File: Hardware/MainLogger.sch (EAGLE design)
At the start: 193 parts, among them J3 GEMS_POWER_PLUGINPUT, J4 U.FL, J5 B_SERIES_M.2EKEY_3042, Q1 DMG3404, Q2 MOSFET_PCH-DMP3036SFG, Q3 MOSFET_PCH-DMP3036SFG, Q4 DMG3404, Q5 NX2301P, U1 FXMAR2102UMLP, U10 SIP32431TDFN, U11 LTC4412S6, U12 TCR2LE31ESV, U13 LP59073.3VYKE, U14 MIC22602, U15 BQ25616, U16 TPS61282D, U17 MCP23018QFN, U18 MCP23018QFN, U19 MAX-M8W, U2 VEML3328, U20 MCP79412SOIC, U21 HALL_EFFECT_SI7201, U22 PCA9634QFN, U23 SN74LVC1G17DCK, U24 TPL5010DDC, U25 TPL5010DDC, U26 MB85RC, U3 MMC5633, U4 MXC6655, U5 PAC1934QFN, U6 PAC1934QFN, U7 SN74AUP1G08DCK, U8 FXMAR2102UMLP, U9 SN74AUP3G34DCU

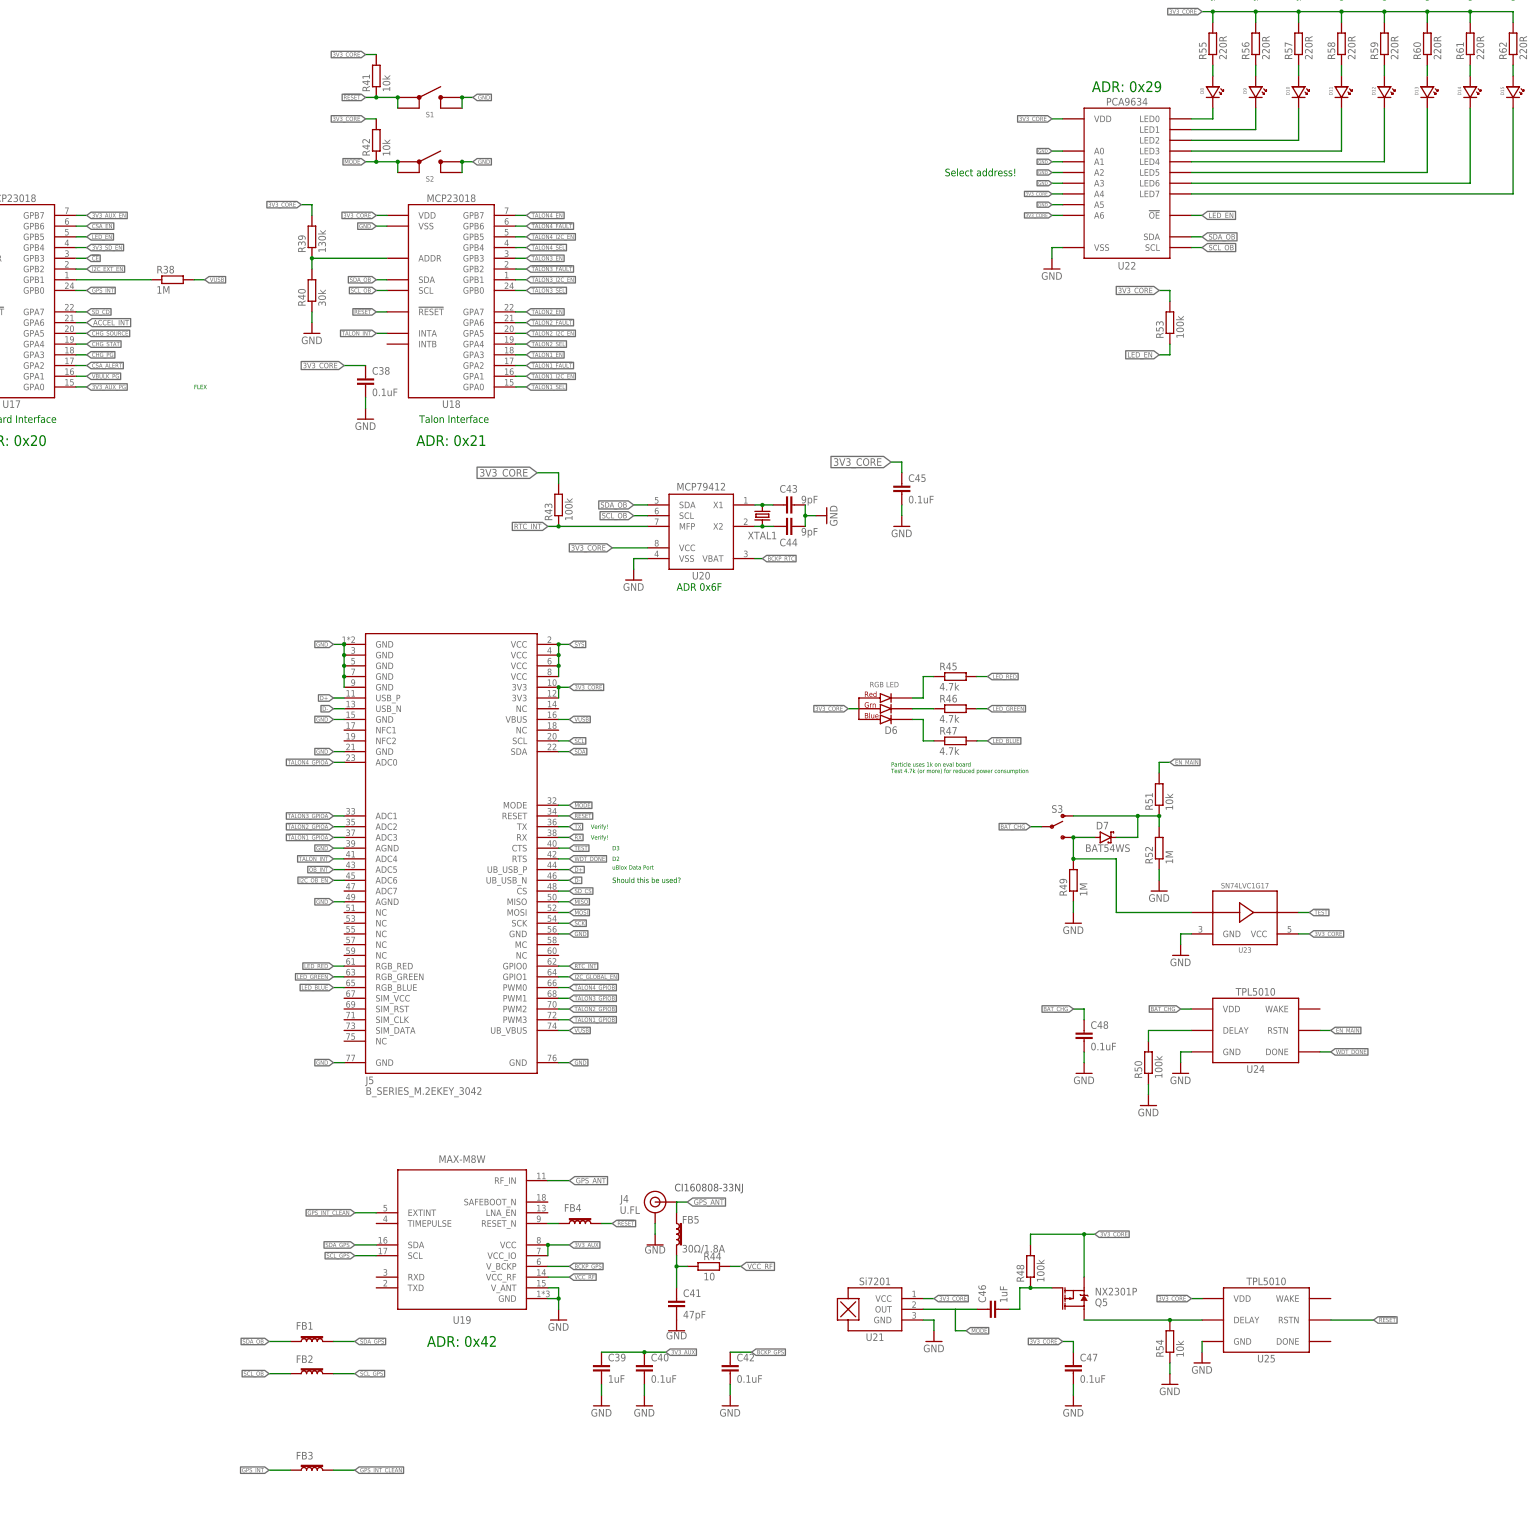
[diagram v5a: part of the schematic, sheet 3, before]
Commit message: v1.0 Update
Many fixes, see ECO and Github issues documentation, v1.0 sent to fab
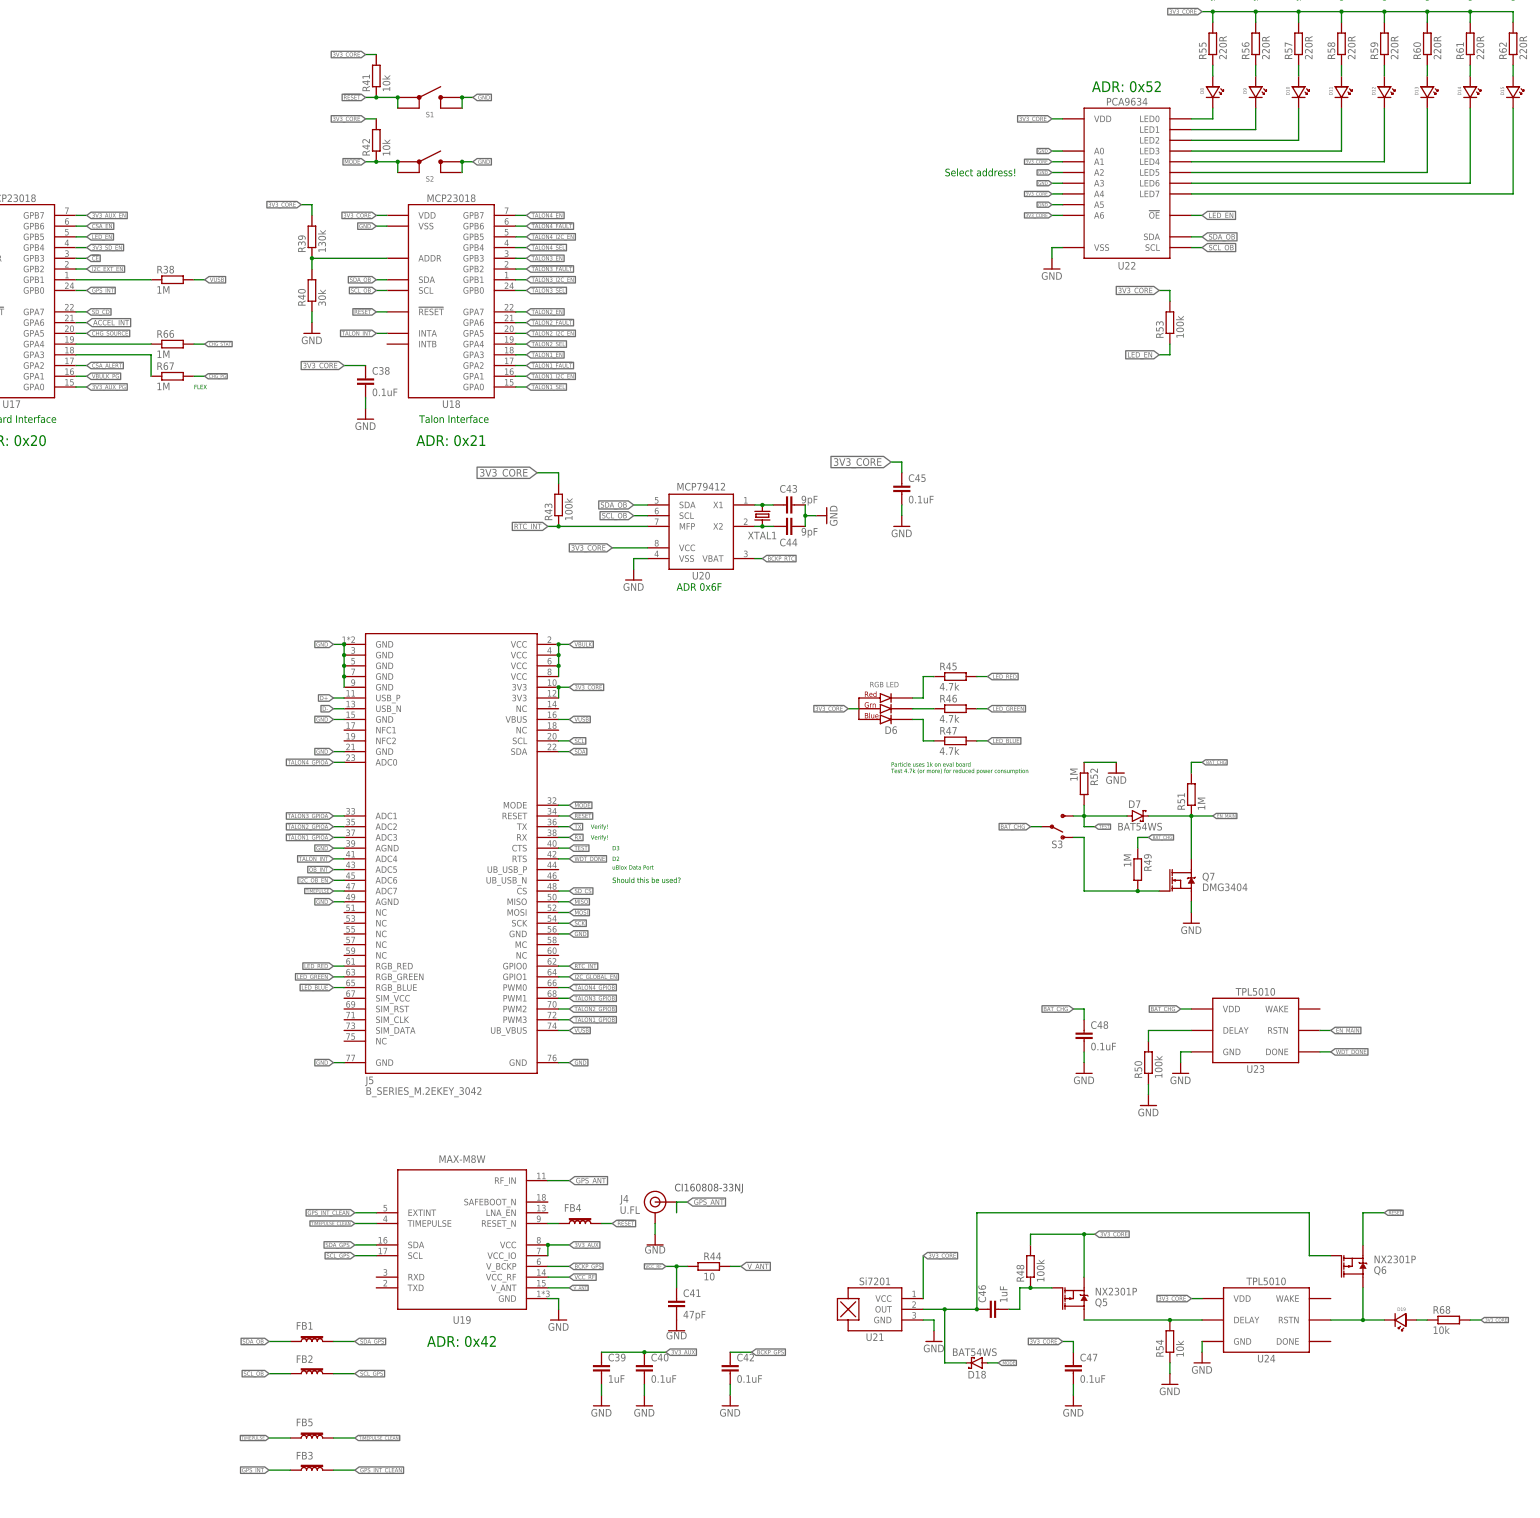
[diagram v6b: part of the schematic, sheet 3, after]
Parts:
- added C50: 0.1uF, bschulz_passives:C-EU0.1UFC0402
- added D17: (no value), bschulz:DIODE_CCBAT54CSOT23
- added D18: BAT54WS, bschulz:DIODE_SCHOTTKYSOD-323
- added D19: LEDGREEN0603, bschulz:LEDGREEN0603
- added Q6: NX2301P, bschulz:MOSFET-PCH-NX2301P
- added Q7: DMG3404, bschulz:MOSFET-NCH-DMG3404L
- added R65, R66, R67: 1M, bschulz_passives:R-EU_1MR0402
- added R68: 10k, bschulz_passives:R-EU_10KR0402
- FB5: value 30Ω/1.8A -> (none); device SparkFun-Coils:FERRITE_BEAD-0603 -> bschulz:FERRITE_BEAD1KS0402; DIGIKEY 445-2986-1-ND -> (none); MF TDK -> (none); MPN MPZ1608D300BTA00 -> (none)
- J3: value GEMS_POWER_PLUGINPUT -> GEMS_POWER_PLUGINPUT_RT; device bschulz:GEMS_POWER_PLUGINPUT -> bschulz:GEMS_POWER_PLUGINPUT_RT
- R51: value 10k -> 1M; device bschulz_passives:R-EU_10KR0402 -> bschulz_passives:R-EU_1MR0402
- S3: value SPDT7103K2CWA -> SPDT7103K2CWAV2; device bschulz:SPDT7103K2CWA -> bschulz:SPDT7103K2CWAV2
- U23: value SN74LVC1G17DCK -> TPL5010DDC; device bschulz:SN74LVC1G17DCK -> bschulz:TPL5010DDC
- U25: value TPL5010DDC -> MB85RC; device bschulz:TPL5010DDC -> bschulz:MB85RC
- U26: value MB85RC -> SHTC3DFN; device bschulz:MB85RC -> bschulz:SHTC3DFN
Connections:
- removed net ANT_VCC: C41.1, FB5.2, R44.1
- removed net N$29: D7.C, R51.1, R52.2, S3.O
- new net N$11: C46.1, D18.C, Q6.G, U21.OUT
- new net N$14: D19.ANODE, R68.1
- new net N$6: R66.1, U17.GPA4
- new net N$8: Q7.G, R49.2, S3.O
- new net N$9: R67.1, U17.GPA3
- new net STAT_CORE: D17.C, R30.2, R31.2, R33.2, R35.2
- new net TIMEPULSE: FB5.1, J5U1.ADC7
- new net TIMEPULSE_CLEAN: FB5.2, U19.TIMEPULSE
- new net V_ANT: R44.2, U19.V_ANT
- net !CHG_PG: now also R67.2; no longer U17.GPA3
- net !MODE: now also D18.A; no longer C46.1, U21.OUT
- net !RESET: now also Q6.S; no longer U25.RSTN
- net 3V3_AUX: now also C50.1, U26.VCC
- net 3V3_CORE: now also D17.A2, R68.2, U22.A1, U24.VDD; no longer U23.VCC, U26.A0, U26.A1, U26.A2, U26.VDD
- net BAT_CHG: now also R49.1, R51.2, U23.VDD; no longer U24.VDD
- net CHG_STAT: now also R66.2; no longer U17.GPA4
- net D+: no longer J5U1.UB_USB_P, U15.D+
- net D-: no longer J5U1.UB_USB_N, U15.D-
- net EN_MAIN: now also D7.C, Q7.D, R51.1, U16.EN, U23.RSTN; no longer R51.2, U24.RSTN
- net GND: now also C50.2, Q7.S, R65.1, U25.A0, U25.A1, U25.A2, U25.VSS, U25.WP, U26.GND; no longer R49.1, U19.V_ANT, U22.A1, U25.GND, U26.VSS, U26.WP
- net GPS_ANT: no longer FB5.1
- net N$12: now also D19.CATHODE, Q6.D, U24.RSTN; no longer D7.A, R49.2, S3.S, U23.A
- net N$30: now also U23.DELAY; no longer U24.DELAY
- net N$32: now also U24.DELAY; no longer U25.DELAY
- net SCL_OB: now also U25.SCL
- net SDA_OB: now also U25.SDA
- net SOLAR+: now also R65.2
- net SYS: no longer J5U1.VCC@2, J5U1.VCC@4, J5U1.VCC@6, J5U1.VCC@8, U16.EN
- net SYSCORE: now also D17.A1; no longer R30.2, R31.2, R33.2, R35.2
- net TEST: now also D7.A, R52.2, S3.S; no longer U23.Y
- net VBULK: now also J5U1.VCC@2, J5U1.VCC@4, J5U1.VCC@6, J5U1.VCC@8
- net VCC_RF: now also C41.1, R44.1; no longer R44.2
- net WDT_DONE: now also U23.DONE; no longer U24.DONE
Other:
- note added: "ADR: 0x52"
- note added: "ADR: 0x70"
- note added: "ALPHA"
- note added: "BETA"
- note added: "C22, C26 Must be 25V!"
- note removed: "ADR: 0x29"
- moved on the sheet: D7, FB5, R10, R49, R51, R52, S3, U24

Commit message: v1.1 Update
Added SIM card, updated pinouts, fixed switch circuit
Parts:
- removed D19: LEDGREEN0603, bschulz:LEDGREEN0603
- removed Q7: DMG3404, bschulz:MOSFET-NCH-DMG3404L
- removed R68: 10k, bschulz_passives:R-EU_10KR0402
- removed TP3, TP4: TESTPOINTRCU, bschulz:TESTPOINTRCU
- added $3_190_$_2021-12-10_02-09-55: B_SERIES_M.2EKEY_3042, Particle-Devices:B_SERIES_M.2EKEY_3042
- added U27: MB85RC, bschulz:MB85RC
- C10, C14, C39, C46: value 1uF -> 0.1uF; device bschulz_passives:C-EU1UFC0603 -> bschulz_passives:C-EU0.1UFC0402
- C11, C40, C47: value 0.1uF -> 1uF; device bschulz_passives:C-EU0.1UFC0402 -> bschulz_passives:C-EU1UFC0603
- C12: value 22uF -> 0.1uF; device bschulz_passives:C-EU22UFC0805 -> bschulz_passives:C-EU0.1UFC0402
- C13: value 0.1uF -> 22uF; device bschulz_passives:C-EU0.1UFC0402 -> bschulz_passives:C-EU22UFC0805
- C15: value 22uF -> 1uF; device bschulz_passives:C-EU22UFC0805 -> bschulz_passives:C-EU1UFC0603
- C18: value 1nF -> 22uF; device bschulz_passives:C-EU1NFC0402 -> bschulz_passives:C-EU22UFC0805
- C19: value 0.1uF -> 1nF; device bschulz_passives:C-EU0.1UFC0402 -> bschulz_passives:C-EU1NFC0402
- C20: value 10nF -> 0.1uF; device bschulz_passives:C-EU10NFC0402 -> bschulz_passives:C-EU0.1UFC0402
- C21: value 1uF -> 10nF; device bschulz_passives:C-EU1UFC0603 -> bschulz_passives:C-EU10NFC0402
- C22: value 10uF -> 1uF; device bschulz_passives:C-EU10UFC0805 -> bschulz_passives:C-EU1UFC0603
- C23: value 39pF -> 10uF; device bschulz_passives:C-EU39PFC0402 -> bschulz_passives:C-EU10UFC0805
- C24: value 10nF -> 39pF; device bschulz_passives:C-EU10NFC0402 -> bschulz_passives:C-EU39PFC0402
- C25: value 100pF -> 10nF; device bschulz_passives:C-EU100PFC0402 -> bschulz_passives:C-EU10NFC0402
- C26: value 1uF -> 100pF; device bschulz_passives:C-EU1UFC0603 -> bschulz_passives:C-EU100PFC0402
- C27: value 100uF -> 1uF; device bschulz_passives:CTANT_EU1411 -> bschulz_passives:C-EU1UFC0603; DIGIKEY 478-5231-1-ND -> (none); MF Kyocera AVX -> (none); MPN TPSB107M010R0400 -> (none)
- C28: value 10uF -> 100uF; device bschulz_passives:C-EU10UFC0805 -> bschulz_passives:CTANT_EU1411; DIGIKEY (none) -> 478-5231-1-ND; MF (none) -> Kyocera AVX; MPN (none) -> TPSB107M010R0400
- C29: value 220uF -> 10uF; device bschulz_passives:CTANT_EU2917 -> bschulz_passives:C-EU10UFC0805; DIGIKEY 399-9744-1-ND -> (none); MF Kemet -> (none); MPN T491D227M010AT -> (none)
- C30: value 1.5uF -> 220uF; device bschulz_passives:C-EU1.5UFC0805 -> bschulz_passives:CTANT_EU2917; DIGIKEY (none) -> 399-9744-1-ND; MF (none) -> Kemet; MPN (none) -> T491D227M010AT
- C31: value 47nF -> 1.5uF; device bschulz_passives:C-EU47PFC0402 -> bschulz_passives:C-EU1.5UFC0805
- C32: value 4.7uF -> 47nF; device bschulz_passives:C-EU4.7UFC0805 -> bschulz_passives:C-EU47PFC0402
- C33: value 10uF -> 4.7uF; device bschulz_passives:C-EU10UFC0805 -> bschulz_passives:C-EU4.7UFC0805
- C37: value 0.1uF -> 10uF; device bschulz_passives:C-EU0.1UFC0402 -> bschulz_passives:C-EU10UFC0805
- C41: value 47pF -> 0.1uF; device bschulz_passives:C-EU47PFC0402 -> bschulz_passives:C-EU0.1UFC0402
- C42: value 0.1uF -> 47pF; device bschulz_passives:C-EU0.1UFC0402 -> bschulz_passives:C-EU47PFC0402
- C43: value 9pF -> 0.1uF; device bschulz_passives:C-EU9PFC0402 -> bschulz_passives:C-EU0.1UFC0402
- C45: value 0.1uF -> 9pF; device bschulz_passives:C-EU0.1UFC0402 -> bschulz_passives:C-EU9PFC0402
- D10, D15: value LEDRED0603 -> LEDGREEN0603; device bschulz:LEDRED0603 -> bschulz:LEDGREEN0603
- D11: value LEDGREEN0603 -> LEDAMBER0603; device bschulz:LEDGREEN0603 -> bschulz:LEDAMBER0603
- D12: value LEDAMBER0603 -> LEDRED0603; device bschulz:LEDAMBER0603 -> bschulz:LEDRED0603
- D16: value RCLAMP3654 -> LEDGREEN0603; device bschulz:RCLAMP3654 -> bschulz:LEDGREEN0603
- D17: value (none) -> LEDAMBER0603; device bschulz:DIODE_CCBAT54CSOT23 -> bschulz:LEDAMBER0603
- D18: value BAT54WS -> LEDRED0603; device bschulz:DIODE_SCHOTTKYSOD-323 -> bschulz:LEDRED0603; DIGIKEY BAT54WS-TPCT-ND -> (none); MF Micro Commercial -> (none); MPN BAT54WS-TP -> (none)
- D2: value CDBA3100 -> RCLAMP3654; device bschulz:DIODE_SCHOTTKYDO-214AC -> bschulz:RCLAMP3654; DIGIKEY 641-1747-1-ND -> (none); MF Comchip -> (none); MPN CDBA3100-HF -> (none)
- D3: value BAT54C -> CDBA3100; device bschulz:DIODE_CCBAT54CSOT23 -> bschulz:DIODE_SCHOTTKYDO-214AC; DIGIKEY (none) -> 641-1747-1-ND; MF (none) -> Comchip; MPN (none) -> CDBA3100-HF
- D4: value LEDGREEN0603 -> BAT54C; device bschulz:LEDGREEN0603 -> bschulz:DIODE_CCBAT54CSOT23
- D5: value LEDAMBER0603 -> LEDGREEN0603; device bschulz:LEDAMBER0603 -> bschulz:LEDGREEN0603
- D6: value CLVBA-FKA -> (none); device bschulz:CLVBA-FKA -> bschulz:DIODE_CCBAT54CSOT23
- D7: value BAT54WS -> LEDAMBER0603; device bschulz:DIODE_SCHOTTKYSOD-323 -> bschulz:LEDAMBER0603; DIGIKEY BAT54WS-TPCT-ND -> (none); MF Micro Commercial -> (none); MPN BAT54WS-TP -> (none)
- D8: value LEDGREEN0603 -> CLVBA-FKA; device bschulz:LEDGREEN0603 -> bschulz:CLVBA-FKA
- D9: value LEDAMBER0603 -> BAT54WS; device bschulz:LEDAMBER0603 -> bschulz:DIODE_SCHOTTKYSOD-323; DIGIKEY (none) -> BAT54WS-TPCT-ND; MF (none) -> Micro Commercial; MPN (none) -> BAT54WS-TP
- J5: value B_SERIES_M.2EKEY_3042 -> SIM_CDNANO_SF72; device Particle-Devices:B_SERIES_M.2EKEY_3042 -> bschulz:SIM_CDNANO_SF72; DIGIKEY A115904CT-ND -> (none); MF TE -> (none); MPN 2199230-4 -> (none)
- R10: value 2m -> 27R; device bschulz_passives:R-EU_0.002R0805 -> bschulz_passives:R-EU_27R0402
- R11: value 1k -> 1M; device bschulz_passives:R-EU_1KR0402 -> bschulz_passives:R-EU_1MR0402
- R12: value 100k -> 1k; device bschulz_passives:R-EU_100KR0402 -> bschulz_passives:R-EU_1KR0402
- R13: value 100k -> 2m; device bschulz_passives:R-EU_100KR0402 -> bschulz_passives:R-EU_0.002R0805
- R14: value 470k -> 100k; device bschulz_passives:R-EU_470KR0603 -> bschulz_passives:R-EU_100KR0402
- R15: value 10m -> 100k; device bschulz_passives:R-EU_0.01R0805 -> bschulz_passives:R-EU_100KR0402
- R16: value 1k -> 470k; device bschulz_passives:R-EU_1KR0603 -> bschulz_passives:R-EU_470KR0603
- R17: value 1M -> 10m; device bschulz_passives:R-EU_1MR0402 -> bschulz_passives:R-EU_0.01R0805
- R18: value 20k -> 1k; device bschulz_passives:R-EU_20KR0402 -> bschulz_passives:R-EU_1KR0603
- R19: value 100k -> 1M; device bschulz_passives:R-EU_100KR0402 -> bschulz_passives:R-EU_1MR0402
- R20: value 10k -> 20k; device bschulz_passives:R-EU_10KR0402 -> bschulz_passives:R-EU_20KR0402
- R21: value 2.7k -> 100k; device bschulz_passives:R-EU_2.7KR0402 -> bschulz_passives:R-EU_100KR0402
- R22: value 0R -> 10k; device bschulz_passives:R-EU_0.0R0402 -> bschulz_passives:R-EU_10KR0402
- R23: value 2m -> 2.7k; device bschulz_passives:R-EU_0.002R0805 -> bschulz_passives:R-EU_2.7KR0402
- R24: value 1M -> 0R; device bschulz_passives:R-EU_1MR0402 -> bschulz_passives:R-EU_0.0R0402
- R25: value 470R -> 2m; device bschulz_passives:R-EU_470R0402 -> bschulz_passives:R-EU_0.002R0805
- R26: value 220R -> 1M; device bschulz_passives:R-EU_220R0402 -> bschulz_passives:R-EU_1MR0402
- R27: value 10k -> 470R; device bschulz_passives:R-EU_10KR0402 -> bschulz_passives:R-EU_470R0402
- R28: value 100k -> 220R; device bschulz_passives:R-EU_100KR0402 -> bschulz_passives:R-EU_220R0402
- R29: value 100k -> 10k; device bschulz_passives:R-EU_100KR0402 -> bschulz_passives:R-EU_10KR0402
- R30: value 1M -> 100k; device bschulz_passives:R-EU_1MR0402 -> bschulz_passives:R-EU_100KR0402
- R31: value 10k -> 100k; device bschulz_passives:R-EU_10KR0402 -> bschulz_passives:R-EU_100KR0402
- R32: value 10m -> 1M; device bschulz_passives:R-EU_0.01R0805 -> bschulz_passives:R-EU_1MR0402
- R33, R65: value 1M -> 10k; device bschulz_passives:R-EU_1MR0402 -> bschulz_passives:R-EU_10KR0402
- R35, R41, R42, R54: value 10k -> 1M; device bschulz_passives:R-EU_10KR0402 -> bschulz_passives:R-EU_1MR0402
- R36: value 150k -> 10m; device bschulz_passives:R-EU_150KR0603 -> bschulz_passives:R-EU_0.01R0805
- R37: device bschulz_passives:R-EU_10KR0603 -> bschulz_passives:R-EU_10KR0402
- R38: value 1M -> 150k; device bschulz_passives:R-EU_1MR0402 -> bschulz_passives:R-EU_150KR0603
- R39: value 130k -> 10k; device bschulz_passives:R-EU_130KR0603 -> bschulz_passives:R-EU_10KR0603
- R40: value 30k -> 1M; device bschulz_passives:R-EU_30KR0603 -> bschulz_passives:R-EU_1MR0402
- R43: value 100k -> 130k; device bschulz_passives:R-EU_100KR0402 -> bschulz_passives:R-EU_130KR0603
- R44: value 10 -> 30k; device bschulz_passives:R-EU_10R0402 -> bschulz_passives:R-EU_30KR0603
- R45, R46: value 4.7k -> 10k; device bschulz_passives:R-EU_4.7KR0603 -> bschulz_passives:R-EU_10KR0402
- R47: value 4.7k -> 100k; device bschulz_passives:R-EU_4.7KR0603 -> bschulz_passives:R-EU_100KR0402
- R48: value 100k -> 10; device bschulz_passives:R-EU_100KR0402 -> bschulz_passives:R-EU_10R0402
- R49: value 1M -> (none); device bschulz_passives:R-EU_1MR0402 -> bschulz_passives:R-EU_100KR0402
- R5: value 10k -> 2m; device bschulz_passives:R-EU_10KR0402 -> bschulz_passives:R-EU_0.002R0805
- R50: value 100k -> 4.7k; device bschulz_passives:R-EU_100KR0402 -> bschulz_passives:R-EU_4.7KR0603
- R51, R52: value 1M -> 4.7k; device bschulz_passives:R-EU_1MR0402 -> bschulz_passives:R-EU_4.7KR0603
- R55: value 220R -> 1M; device bschulz_passives:R-EU_220R0603 -> bschulz_passives:R-EU_1MR0402
- R56, R57: value 220R -> 100k; device bschulz_passives:R-EU_220R0603 -> bschulz_passives:R-EU_100KR0402
- R58: value 220R -> 10k; device bschulz_passives:R-EU_220R0603 -> bschulz_passives:R-EU_10KR0402
- R59, R60, R61, R62: device bschulz_passives:R-EU_220R0603 -> bschulz_passives:R-EU_220R0402
- R63, R64: value 27R -> 220R; device bschulz_passives:R-EU_27R0402 -> bschulz_passives:R-EU_220R0402
- R66, R67: value 1M -> 220R; device bschulz_passives:R-EU_1MR0402 -> bschulz_passives:R-EU_220R0402
- R8: value 2m -> 100k; device bschulz_passives:R-EU_0.002R0805 -> bschulz_passives:R-EU_100KR0402
- R9: value 100k -> 27R; device bschulz_passives:R-EU_100KR0402 -> bschulz_passives:R-EU_27R0402
- U10: value SIP32431TDFN -> SN74AUP3G34DCU; device bschulz:SIP32431TDFN -> bschulz:SN74AUP3G34DCU
- U11: value LTC4412S6 -> SIP32431TDFN; device bschulz:LTC4412S6 -> bschulz:SIP32431TDFN
- U12: value TCR2LE31ESV -> LTC4412S6; device bschulz:TCR2LE31ESV -> bschulz:LTC4412S6
- U13: value LP59073.3VYKE -> TCR2LE31ESV; device bschulz:LP59073.3VYKE -> bschulz:TCR2LE31ESV
- U14: value MIC22602 -> LP59073.3VYKE; device bschulz:MIC22602 -> bschulz:LP59073.3VYKE
- U15: value BQ25616 -> MIC22602; device bschulz:BQ25616 -> bschulz:MIC22602
- U16: value TPS61282D -> BQ25616; device bschulz:TPS61282D -> bschulz:BQ25616
- U17: value MCP23018QFN -> TPS61282D; device bschulz:MCP23018QFN -> bschulz:TPS61282D
- U19: value MAX-M8W -> MCP23018QFN; device bschulz:MAX-M8W -> bschulz:MCP23018QFN
- U20: value MCP79412SOIC -> MAX-M8W; device bschulz:MCP79412SOIC -> bschulz:MAX-M8W
- U21: value HALL_EFFECT_SI7201 -> MCP79412SOIC; device bschulz:HALL_EFFECT_SI7201 -> bschulz:MCP79412SOIC
- U22: value PCA9634QFN -> HALL_EFFECT_SI7201; device bschulz:PCA9634QFN -> bschulz:HALL_EFFECT_SI7201
- U23: value TPL5010DDC -> PCA9634QFN; device bschulz:TPL5010DDC -> bschulz:PCA9634QFN
- U24: value TPL5010DDC -> SN74LVC1G17DCK; device bschulz:TPL5010DDC -> bschulz:SN74LVC1G17DCK
- U25: value MB85RC -> TPL5010DDC; device bschulz:MB85RC -> bschulz:TPL5010DDC
- U26: value SHTC3DFN -> TPL5010DDC; device bschulz:SHTC3DFN -> bschulz:TPL5010DDC
- U7: value SN74AUP1G08DCK -> SHTC3DFN; device bschulz:SN74AUP1G08DCK -> bschulz:SHTC3DFN
- U8: value FXMAR2102UMLP -> SN74AUP1G08DCK; device bschulz:FXMAR2102UMLP -> bschulz:SN74AUP1G08DCK
- U9: value SN74AUP3G34DCU -> FXMAR2102UMLP; device bschulz:SN74AUP3G34DCU -> bschulz:FXMAR2102UMLP
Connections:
- removed net ACCEL_INT: R5.1, U17.GPA6, U4.INT
- removed net CSA_ALERT: R2.1, U17.GPA2, U5.SLOW/!ALERT, U6.SLOW/!ALERT
- removed net N$15: R38.1, U17.GPB1
- new net EN_MAIN_OD: R55.2, S3.O, U24.A, U25.RSTN
- new net SENSOR_INT: R2.1, U18.GPA2, U4.INT, U5.SLOW/!ALERT, U6.SLOW/!ALERT
- new net SIM_CD: J5.SW, R49.1, U18.GPB1
- new net SIM_CLK: $3_190_$_2021-12-10_02-09-55U1.SIM_CLK, J5.CLK
- new net SIM_DATA: $3_190_$_2021-12-10_02-09-55U1.SIM_DATA, J5.I/O
- new net SIM_RST: $3_190_$_2021-12-10_02-09-55U1.SIM_RST, J5.RST
- new net SIM_VCC: $3_190_$_2021-12-10_02-09-55U1.SIM_VCC, J5.VCC
- net !CE: now also R24.1, U18.GPB3; no longer R22.1, U17.GPB3
- net !CHG_PG: now also D7.CATHODE, R35.1, R42.2, U16.!PG; no longer D5.CATHODE, R33.1, R67.2, U15.!PG
- net !MODE: now also $3_190_$_2021-12-10_02-09-55U1.MODE, D9.A, R46.1; no longer D18.A, J5U1.MODE, R42.1
- net !RESET: now also $3_190_$_2021-12-10_02-09-55U1.RESET, FB5.2, R45.1, U19.!RESET; no longer FB4.2, J5U1.RESET, R41.1, U17.!RESET
- net !TALON1_FAULT: now also U19.GPA2; no longer U18.GPA2
- net !TALON2_FAULT: now also U19.GPA6; no longer U18.GPA6
- net !TALON3_FAULT: now also U19.GPB2; no longer U18.GPB2
- net !TALON4_FAULT: now also U19.GPB6; no longer U18.GPB6
- net 3V3_AUX: now also C11.1, C41.1, C9.1, R6.1, U11.VIN, U20.VCC, U20.VCC_IO, U7.VCC; no longer C10.1, C39.1, C50.1, R7.1, U10.VIN, U19.VCC, U19.VCC_IO, U26.VCC
- net 3V3_AUX_EN: now also R15.1, U15.EN/DLY, U18.GPB7; no longer R13.1, U14.EN/DLY, U17.GPB7
- net 3V3_AUX_PG: now also R21.1, U15.POR/PG, U18.GPA0; no longer R19.1, U14.POR/PG, U17.GPA0
- net 3V3_BULK: now also R7.1; no longer R8.1
- net 3V3_BULK+: now also C25.1, C28.+, R21.2, R22.2, R6.2; no longer C24.1, C27.+, R19.2, R20.2, R8.2
- net 3V3_CORE: now also $3_190_$_2021-12-10_02-09-55U1.3V3@10, $3_190_$_2021-12-10_02-09-55U1.3V3@12, C10.1, C39.1, C46.1, C48.1, C50.1, D6.A2, D8.ANODE, R19.2, R38.2, R45.2, R46.2, R47.2, R49.2, R63.2, R64.2, R65.2, R66.2, R67.2, U19.VDD, U22.VCC, U23.A1, U23.A4, U23.A6, U23.VDD, U26.VDD, U27.VDD, U8.VCC, U9.VA, U9.VB; no longer C37.1, C45.1, C47.1, C49.1, C9.1, D17.A2, D6.ANODE, J5U1.3V3@10, J5U1.3V3@12, R13.2, R36.2, R39.2, R41.2, R42.2, R48.2, R5.2, R55.2, R56.2, R58.2, R68.2, U17.VDD, U20.VCC, U22.A1, U22.A4, U22.A6, U22.VDD, U24.VDD, U25.VDD, U7.VCC, U8.VA, U8.VB
- net 3V3_CORE+: now also C22.1, R17.1, U14.VOUT; no longer C21.1, R15.1, U13.VOUT
- net 3V3_SD: now also C12.1, R8.2, U10.VCC, U11.VOUT; no longer C11.1, R9.2, U10.VOUT, U9.VCC
- net 3V3_SD_EN: now also R14.2, U11.EN, U18.GPB4; no longer R12.2, U10.EN, U17.GPB4
- net BAT: now also R34.2; no longer R32.2
- net BAT_CHG: now also C34.1, C49.1, D4.A2, R34.1, R54.1, R55.1, U16.BAT, U24.VCC, U25.VDD; no longer C33.1, C48.1, D3.A2, R32.1, R49.1, R51.2, S3.P, U15.BAT, U23.VDD
- net BCKP_GPS: now also C43.1, D4.A1, R18.2, U20.V_BCKP; no longer C42.1, D3.A1, R16.2, U19.V_BCKP
- net BCKP_RTC: now also D4.C, U21.VBAT; no longer D3.C, U20.VBAT
- net BTST: now also C32.2, U16.BTST; no longer C31.2, U15.BTST
- net CHG_SOURCE: now also R19.1, U18.GPA6; no longer R17.1, U17.GPA5
- net CHG_STAT: now also D5.CATHODE, R32.1, R41.2, U16.STAT; no longer D4.CATHODE, R30.1, R66.2, U15.STAT
- net COMP: now also C24.1, U15.COMP; no longer C23.1, U14.COMP
- net CSA_EN: now also U18.GPB6; no longer U17.GPB6
- net D+: now also $3_190_$_2021-12-10_02-09-55U1.USB_P, R9.1; no longer J5U1.USB_P, R63.1
- net D+_IN: now also D2.D+, R9.2; no longer D16.D+, R63.2
- net D-: now also $3_190_$_2021-12-10_02-09-55U1.USB_N, R10.1; no longer J5U1.USB_N, R64.1
- net D-_IN: now also D2.D-, R10.2; no longer D16.D-, R64.2
- net DELAY: now also C21.1, U15.DELAY; no longer C20.1, U14.DELAY
- net EN_MAIN: now also U17.EN, U24.Y; no longer D7.C, Q7.D, R51.1, U16.EN, U23.RSTN
- net FAULT_BUS: now also R12.2; no longer R11.2
- net FB: now also C25.2, C26.1, R22.1, R23.2, U15.FB; no longer C24.2, C25.1, R20.1, R21.2, U14.FB
- net GND: now also $3_190_$_2021-12-10_02-09-55U1.AGND@39, $3_190_$_2021-12-10_02-09-55U1.AGND@49, $3_190_$_2021-12-10_02-09-55U1.GND@1, $3_190_$_2021-12-10_02-09-55U1.GND@15, $3_190_$_2021-12-10_02-09-55U1.GND@21, $3_190_$_2021-12-10_02-09-55U1.GND@3, $3_190_$_2021-12-10_02-09-55U1.GND@5, $3_190_$_2021-12-10_02-09-55U1.GND@56, $3_190_$_2021-12-10_02-09-55U1.GND@7, $3_190_$_2021-12-10_02-09-55U1.GND@76, $3_190_$_2021-12-10_02-09-55U1.GND@77, $3_190_$_2021-12-10_02-09-55U1.GND@9, C23.2, C27.2, C28.-, C29.2, C30.-, C31.2, C46.2, D2.GND, D3.A, J5.GND, R11.1, R14.1, R20.1, R23.1, R27.1, R28.1, R29.2, R31.1, R39.1, R44.1, R56.1, R58.1, S3.P, U12.CTL, U14.GND, U15.SGND, U16.OTG, U17.AGND, U17.MODE, U17.PGND, U19.VSS, U20.GND, U21.VSS, U22.GND, U23.A0, U23.A2, U23.A3, U23.A5, U23.VSS, U25.GND, U27.A0, U27.A1, U27.A2, U27.VSS, U27.WP; no longer C25.2, C27.-, C28.2, C29.-, C30.2, C32.2, C47.2, D16.GND, D2.A, J5U1.AGND@39, J5U1.AGND@49, J5U1.GND@1, J5U1.GND@15, J5U1.GND@21, J5U1.GND@3, J5U1.GND@5, J5U1.GND@56, J5U1.GND@7, J5U1.GND@76, J5U1.GND@77, J5U1.GND@9, Q7.S, R12.1, R18.1, R21.1, R24.1, R25.1, R27.2, R29.1, R37.1, R40.1, R50.1, R52.1, R54.1, R65.1, U11.CTL, U14.PGND, U14.SGND, U15.OTG, U16.AGND, U16.MODE, U17.VSS, U19.GND, U20.VSS, U21.GND, U22.A0, U22.A2, U22.A3, U22.A5, U22.VSS, U23.GND, U25.A0, U25.A1, U25.A2, U25.VSS, U25.WP
- net GPS_ANT: now also U20.RF_IN; no longer U19.RF_IN
- net GPS_INT: now also FB4.1, U18.GPA7; no longer FB3.1, U17.GPB0
- net GPS_INT_CLEAN: now also FB4.2, U20.EXTINT; no longer FB3.2, U19.EXTINT
- net I2C_EXT_EN: now also U18.GPB2, U8.B; no longer U17.GPB2, U7.B
- net I2C_EXT_EN_OUT: now also U8.Y, U9.EN; no longer U7.Y, U8.EN
- net I2C_GLOBAL_EN: now also $3_190_$_2021-12-10_02-09-55U1.GPIO1, U8.A; no longer J5U1.GPIO1, U7.A
- net I2C_OB_EN: now also $3_190_$_2021-12-10_02-09-55U1.ADC6; no longer J5U1.ADC6
- net ICHG: now also R28.2, U16.ICHG; no longer R26.2, U15.ICHG
- net ILIM: now also R27.2, U16.ILIM; no longer R25.2, U15.ILIM
- net LED_BLUE: now also $3_190_$_2021-12-10_02-09-55U1.RGB_BLUE, R52.2; no longer J5U1.RGB_BLUE, R47.2
- net LED_EN: now also R57.1, U18.GPB5, U23.!OE; no longer R53.1, U17.GPB5, U22.!OE
- net LED_GREEN: now also $3_190_$_2021-12-10_02-09-55U1.RGB_GREEN, R51.2; no longer J5U1.RGB_GREEN, R46.2
- net LED_RED: now also $3_190_$_2021-12-10_02-09-55U1.RGB_RED, R50.2; no longer J5U1.RGB_RED, R45.2
- net MISO: now also $3_190_$_2021-12-10_02-09-55U1.MISO; no longer J5U1.MISO
- net MOSI: now also $3_190_$_2021-12-10_02-09-55U1.MOSI, U10.1A; no longer J5U1.MOSI, U9.1A
- net MOSI_BUF: now also U10.1Y; no longer U9.1Y
- net N$10: now also R26.2, U16.!CE; no longer R22.2, U15.!CE
- net N$11: now also C47.1, D9.C, U22.OUT; no longer C46.1, D18.C, U21.OUT
- net N$12: now also D15.CATHODE, U26.RSTN; no longer D19.CATHODE, U24.RSTN
- net N$13: now also C47.2, R53.1; no longer C46.2, R48.1
- net N$14: now also D15.ANODE, R65.1; no longer D19.ANODE, R68.1
- net N$18: now also D7.ANODE, R37.1; no longer D5.ANODE, R35.1
- net N$20: now also D5.ANODE, R33.1; no longer D4.ANODE, R31.1
- net N$21: now also D8.BLUE_CATH, R52.1; no longer D6.BLUE_CATH, R47.1
- net N$22: now also D8.GREEN_CATH, R51.1; no longer D6.GREEN_CATH, R46.1
- net N$23: now also D8.RED_CATH, R50.1; no longer D6.RED_CATH, R45.1
- net N$24: now also FB5.1, U20.RESET_N; no longer FB4.1, U19.RESET_N
- net N$25: now also R12.1; no longer R11.1
- net N$3: now also C20.1, R18.1, U13.VOUT; no longer C19.1, R16.1, U12.VOUT
- net N$30: now also R56.2, U25.DELAY; no longer R50.2, U23.DELAY
- net N$32: now also R58.2, U26.DELAY; no longer R54.2, U24.DELAY
- net N$33: now also C24.2, R20.2; no longer C23.2, R18.2
- net N$35: now also R43.1, R44.2, U19.ADDR; no longer R39.1, R40.2, U18.ADDR
- net N$36: now also D10.CATHODE, U23.LED0; no longer D8.CATHODE, U22.LED0
- net N$37: now also D11.CATHODE, U23.LED1; no longer D9.CATHODE, U22.LED1
- net N$38: now also R38.1, R39.2, U18.ADDR; no longer R36.1, R37.2, U17.ADDR
- net N$39: now also D12.CATHODE, U23.LED2; no longer D10.CATHODE, U22.LED2
- net N$4: now also C44.1, U21.X1; no longer C43.1, U20.X1
- net N$40: now also D13.CATHODE, U23.LED3; no longer D11.CATHODE, U22.LED3
- net N$41: now also D14.CATHODE, U23.LED4; no longer D12.CATHODE, U22.LED4
- net N$42: now also D16.CATHODE, U23.LED5; no longer D13.CATHODE, U22.LED5
- net N$43: now also D17.CATHODE, U23.LED6; no longer D14.CATHODE, U22.LED6
- net N$44: now also D18.CATHODE, U23.LED7; no longer D15.CATHODE, U22.LED7
- net N$45: now also D10.ANODE, R59.1; no longer D8.ANODE, R55.1
- net N$46: now also D11.ANODE, R60.1; no longer D9.ANODE, R56.1
- net N$47: now also D12.ANODE, R61.1; no longer D10.ANODE, R57.1
- net N$48: now also D13.ANODE, R62.1; no longer D11.ANODE, R58.1
- net N$49: now also D14.ANODE, R63.1; no longer D12.ANODE, R59.1
- net N$5: now also U12.GATE; no longer U11.GATE
- net N$50: now also D16.ANODE, R64.1; no longer D13.ANODE, R60.1
- net N$51: now also D17.ANODE, R66.1; no longer D14.ANODE, R61.1
- net N$52: now also D18.ANODE, R67.1; no longer D15.ANODE, R62.1
- net N$6: now also R41.1, U18.GPA4; no longer R66.1, U17.GPA4
- net N$7: now also C45.1, U21.X2; no longer C44.1, U20.X2
- net N$8: now also R40.1, U18.GPA5; no longer Q7.G, R49.2, S3.O
- net N$9: now also R42.1, U18.GPA3; no longer R67.1, U17.GPA3
- net OB_INT: now also $3_190_$_2021-12-10_02-09-55U1.ADC5, U18.INTA; no longer J5U1.ADC5, U17.INTA
- net PMID: now also C29.1, U16.PMID; no longer C28.1, U15.PMID
- net RC: now also C19.1, U15.RC; no longer C18.1, U14.RC
- net REGN: now also C33.1, R30.2, U16.REGN; no longer C32.1, R28.2, U15.REGN
- net RTC_INT: now also $3_190_$_2021-12-10_02-09-55U1.GPIO0, R47.1, U21.MFP; no longer J5U1.GPIO0, R43.1, U20.MFP
- net RX: now also $3_190_$_2021-12-10_02-09-55U1.RX; no longer J5U1.RX
- net SCK: now also $3_190_$_2021-12-10_02-09-55U1.SCK, U10.2A; no longer J5U1.SCK, U9.2A
- net SCK_BUF: now also U10.2Y; no longer U9.2Y
- net SCL: now also $3_190_$_2021-12-10_02-09-55U1.SCL, U9.A2; no longer J5U1.SCL, U8.A2
- net SCL_EXT: now also U9.B2; no longer U8.B2
- net SCL_GPS: now also U20.SCL; no longer U19.SCL
- net SCL_OB: now also U19.SCL, U21.SCL, U23.SCL, U27.SCL, U7.SCL; no longer TP4.P$1, U17.SCL, U20.SCL, U22.SCL, U25.SCL, U26.SCL
- net SDA: now also $3_190_$_2021-12-10_02-09-55U1.SDA, U9.A1; no longer J5U1.SDA, U8.A1
- net SDA_EXT: now also U9.B1; no longer U8.B1
- net SDA_GPS: now also U20.SDA; no longer U19.SDA
- net SDA_OB: now also U19.SDA, U21.SDA, U23.SDA, U27.SDA, U7.SDA; no longer TP3.P$1, U17.SDA, U20.SDA, U22.SDA, U25.SDA, U26.SDA
- net SD_CD: now also R8.1, U18.GPB0; no longer R9.1, U17.GPA7
- net SD_CS: now also $3_190_$_2021-12-10_02-09-55U1.CS, U10.3A; no longer J5U1.CS, U9.3A
- net SD_CS_BUF: now also U10.3Y; no longer U9.3Y
- net SOLAR+: now also R11.2, R13.1; no longer R10.1, R65.2
- net STAT_CORE: now also D6.C, R32.2, R37.2; no longer D17.C, R30.2, R31.2
- net ST_CORE: now also R16.1, U12.STAT; no longer R14.1, U11.STAT
- net SW: now also C32.1, U16.SW; no longer C31.1, U15.SW
- net SW1: now also D3.C, U15.SW; no longer D2.C, U14.SW
- net SW2: now also U17.SW; no longer U16.SW
- net SYS: now also C14.1, C30.+, C31.1, R36.2, U13.EN, U13.VIN, U17.!BYP, U17.VIN, U17.VSEL; no longer C13.1, C29.+, C30.1, R34.2, U12.EN, U12.VIN, U16.!BYP, U16.VIN, U16.VSEL
- net SYSCORE: now also C36.1, D6.A1, R36.1, U16.SYS; no longer C35.1, D17.A1, R34.1, U15.SYS
- net TALON1_EN: now also U19.GPA3; no longer U18.GPA3
- net TALON1_GPIOA: now also $3_190_$_2021-12-10_02-09-55U1.ADC3; no longer J5U1.ADC3
- net TALON1_GPIOB: now also $3_190_$_2021-12-10_02-09-55U1.PWM3; no longer J5U1.PWM3
- net TALON1_I2C_EN: now also U19.GPA1; no longer U18.GPA1
- net TALON1_SEL: now also U19.GPA0; no longer U18.GPA0
- net TALON2_EN: now also U19.GPA7; no longer U18.GPA7
- net TALON2_GPIOA: now also $3_190_$_2021-12-10_02-09-55U1.ADC2; no longer J5U1.ADC2
- net TALON2_GPIOB: now also $3_190_$_2021-12-10_02-09-55U1.PWM2; no longer J5U1.PWM2
- net TALON2_I2C_EN: now also U19.GPA5; no longer U18.GPA5
- net TALON2_SEL: now also U19.GPA4; no longer U18.GPA4
- net TALON3_EN: now also U19.GPB3; no longer U18.GPB3
- net TALON3_GPIOA: now also $3_190_$_2021-12-10_02-09-55U1.ADC1; no longer J5U1.ADC1
- net TALON3_GPIOB: now also $3_190_$_2021-12-10_02-09-55U1.PWM1; no longer J5U1.PWM1
- net TALON3_I2C_EN: now also U19.GPB1; no longer U18.GPB1
- net TALON3_SEL: now also U19.GPB0; no longer U18.GPB0
- net TALON4_EN: now also U19.GPB7; no longer U18.GPB7
- net TALON4_GPIOA: now also $3_190_$_2021-12-10_02-09-55U1.ADC0; no longer J5U1.ADC0
- net TALON4_GPIOB: now also $3_190_$_2021-12-10_02-09-55U1.PWM0; no longer J5U1.PWM0
- net TALON4_I2C_EN: now also U19.GPB5; no longer U18.GPB5
- net TALON4_SEL: now also U19.GPB4; no longer U18.GPB4
- net TALON_INT: now also $3_190_$_2021-12-10_02-09-55U1.ADC4, U19.INTA; no longer J5U1.ADC4, U18.INTA
- net TEST: now also $3_190_$_2021-12-10_02-09-55U1.CTS, R54.2; no longer D7.A, J5U1.CTS, R52.2
- net TIMEPULSE: now also $3_190_$_2021-12-10_02-09-55U1.ADC7, FB3.1; no longer FB5.1, J5U1.ADC7
- net TIMEPULSE_CLEAN: now also FB3.2, U20.TIMEPULSE; no longer FB5.2, U19.TIMEPULSE
- net TS: now also R30.1, R31.2, U16.TS; no longer R28.1, R29.2, U15.TS
- net TX: now also $3_190_$_2021-12-10_02-09-55U1.TX; no longer J5U1.TX
- net VBULK: now also $3_190_$_2021-12-10_02-09-55U1.VCC@2, $3_190_$_2021-12-10_02-09-55U1.VCC@4, $3_190_$_2021-12-10_02-09-55U1.VCC@6, $3_190_$_2021-12-10_02-09-55U1.VCC@8, C13.1, C18.1, R5.1, U14.EN, U14.VIN, U15.PVIN, U15.SVIN; no longer C12.1, C14.1, J5U1.VCC@2, J5U1.VCC@4, J5U1.VCC@6, J5U1.VCC@8, R6.1, U13.EN, U13.VIN, U14.PVIN, U14.SVIN
- net VBULK+: now also C35.1, C37.1, R5.2, U17.VOUT; no longer C34.1, C36.1, R6.2, U16.VOUT
- net VBULK_PG: now also U17.PG, U18.GPA1; no longer U16.PG, U17.GPA1
- net VBUS: now also C27.1, R25.2, U16.VAC, U16.VBUS; no longer C26.1, R23.2, U15.VAC, U15.VBUS
- net VCC_RF: now also C42.1, R48.1, U20.VCC_RF; no longer C41.1, R44.1, U19.VCC_RF
- net VPRIME: now also C23.1, R16.2, R25.1, U12.SENSE; no longer C22.1, R14.2, R23.1, U11.SENSE
- net VSET: now also R29.1, U16.VSET; no longer R27.1, U15.VSET
- net VSOLAR: now also R13.2, U12.VIN; no longer R10.2, U11.VIN
- net VUSB: now also $3_190_$_2021-12-10_02-09-55U1.VBUS, D2.VBUS, R40.2; no longer D16.VBUS, J5U1.UB_VBUS, J5U1.VBUS, R38.2
- net V_ANT: now also R48.2, U20.V_ANT; no longer R44.2, U19.V_ANT
- net WDT_DONE: now also $3_190_$_2021-12-10_02-09-55U1.RTS, U25.DONE; no longer J5U1.RTS, U23.DONE
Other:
- note added: "DNP and use internal pullup on IO exp to reduce Iq"

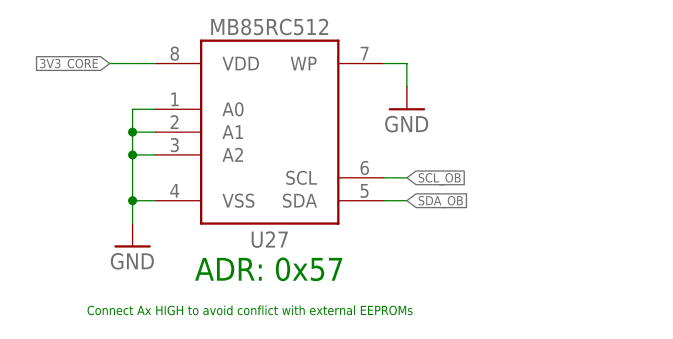
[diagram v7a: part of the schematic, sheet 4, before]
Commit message: Updated address note and added renumber file
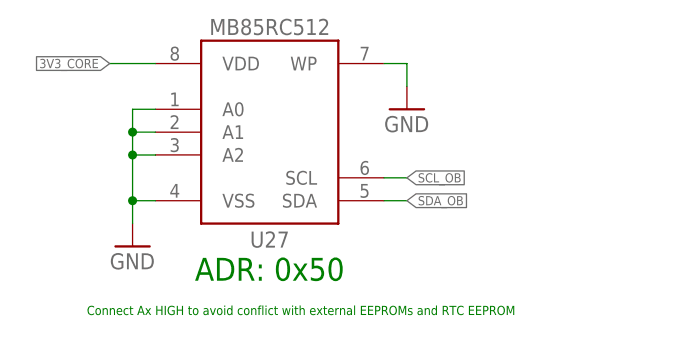
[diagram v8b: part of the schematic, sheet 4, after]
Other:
- note added: "ADR: 0x50"
- note added: "Connect Ax HIGH to avoid conflict with external EEPROMs and RTC EEPROM"
- note removed: "ADR: 0x57"
- note removed: "Connect Ax HIGH to avoid conflict with external EEPROMs"
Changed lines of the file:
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@@
 <plain>
 <text x="12.7" y="101.6" size="1.016" layer="91">Should this be 3V3_AUX?</text>
-<text x="20.32" y="40.64" size="1.016" layer="91">Connect Ax HIGH to avoid conflict with external EEPROMs</text>
-<text x="40.64" y="45.72" size="2.54" layer="91" align="center">ADR: 0x57</text>
+<text x="20.32" y="40.64" size="1.016" layer="91">Connect Ax HIGH to avoid conflict with external EEPROMs and RTC EEPROM</text>
+<text x="40.64" y="45.72" size="2.54" layer="91" align="center">ADR: 0x50</text>
 </plain>
 <instances>
